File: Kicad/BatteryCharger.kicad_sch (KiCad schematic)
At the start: 25 parts, among them IC1 FS312F-G, Q30 FS8205

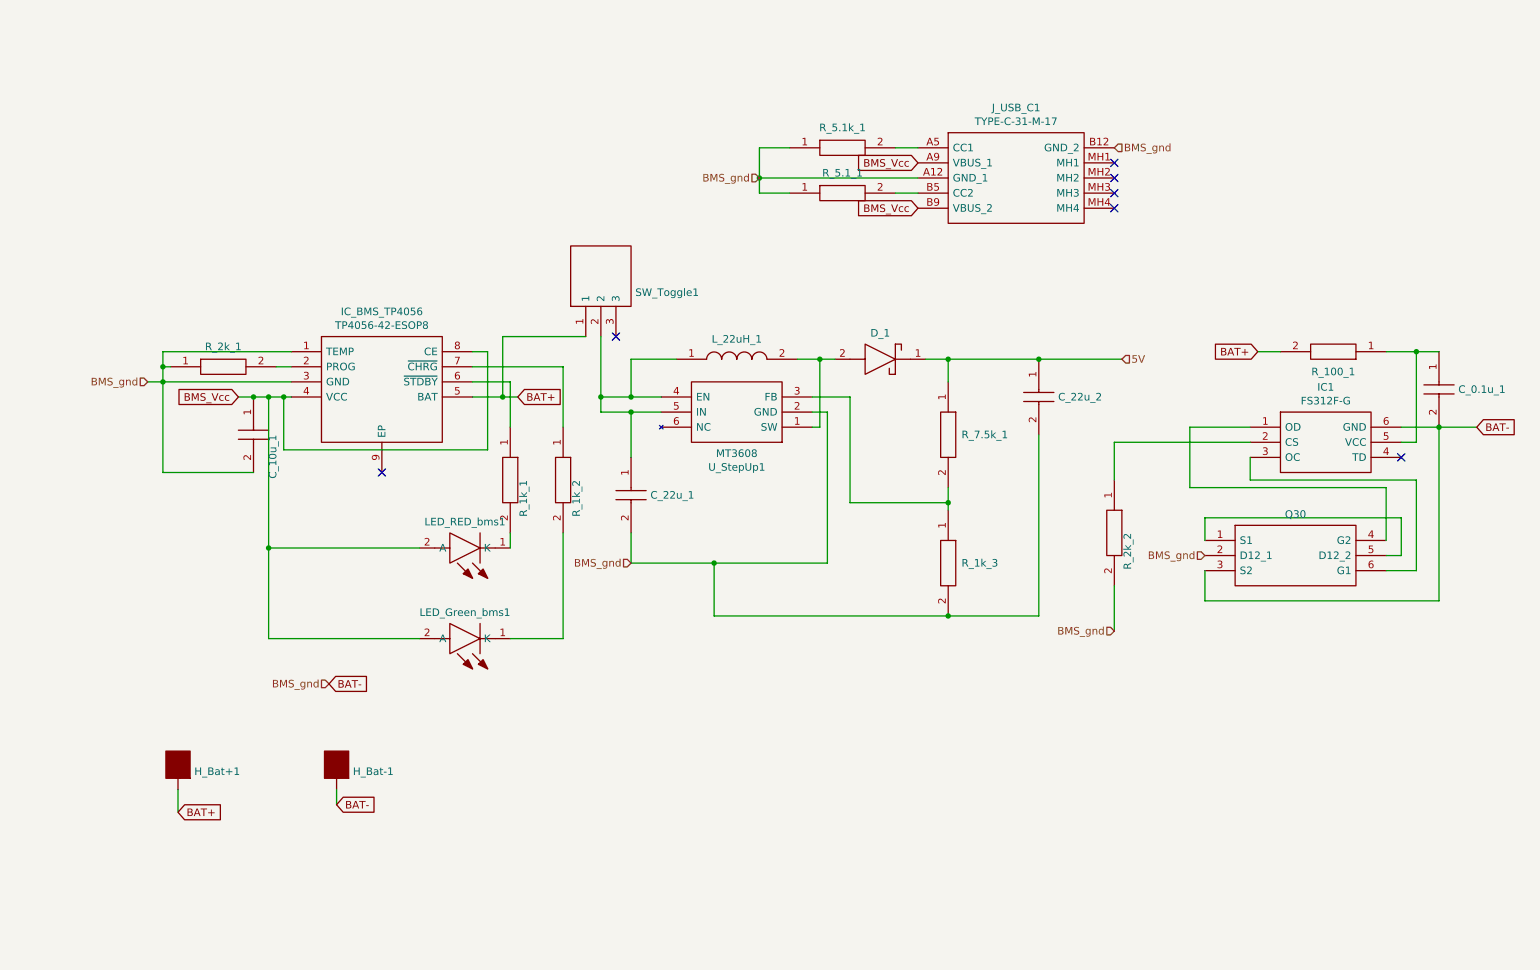
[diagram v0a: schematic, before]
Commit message: New V1.2 Hardware Release
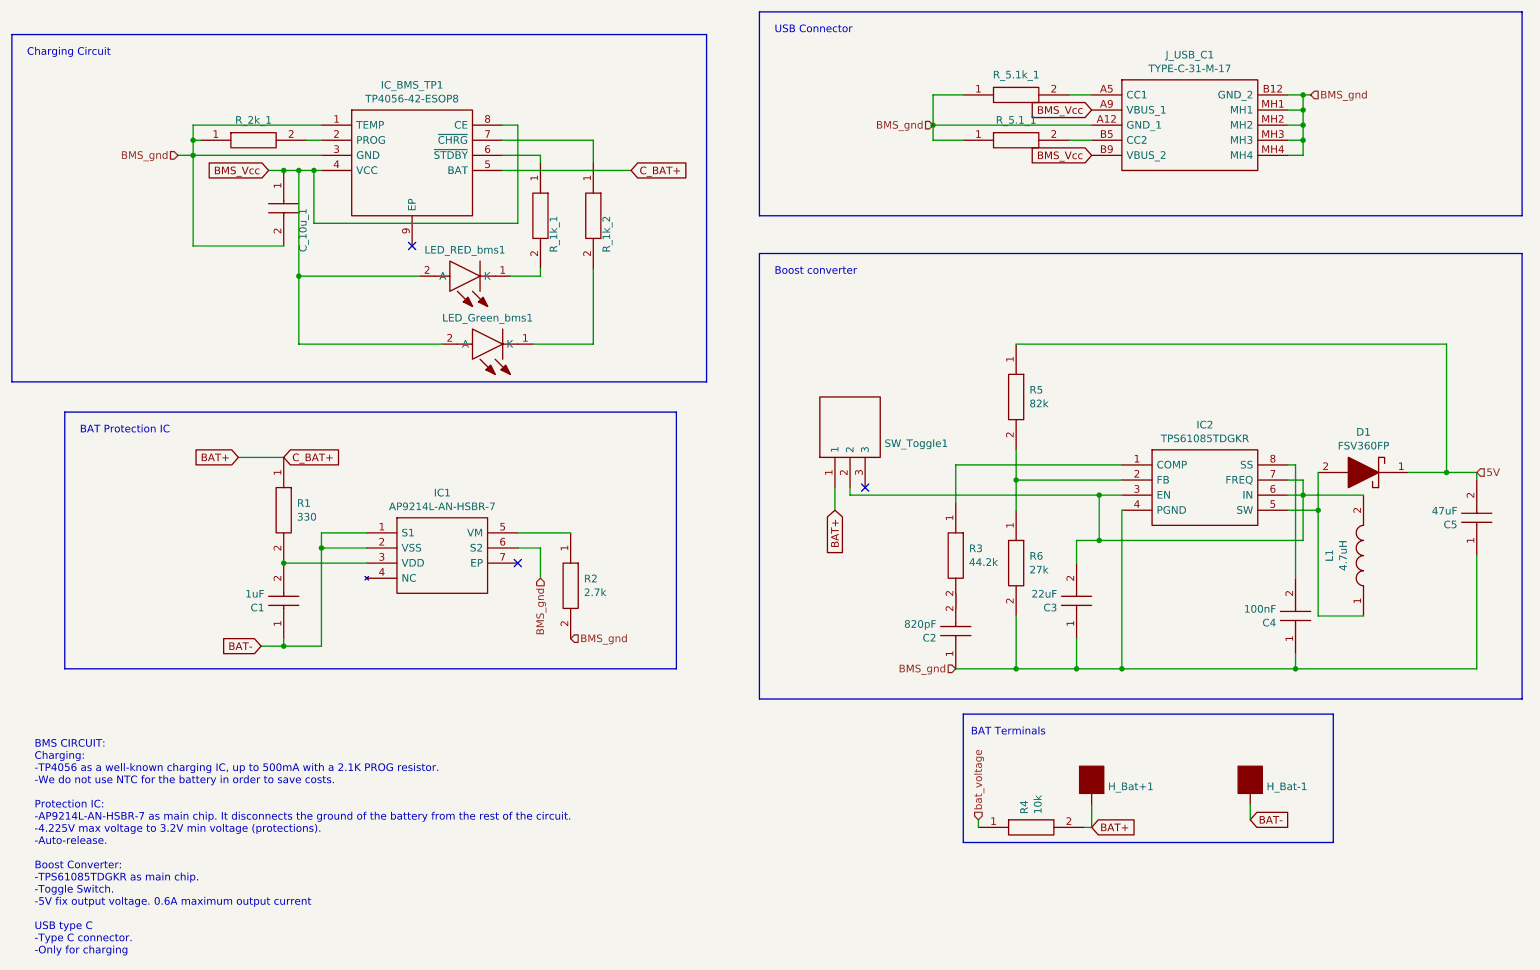
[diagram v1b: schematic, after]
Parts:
- removed C_0.1u_1, C_22u_1, C_22u_2: GCG21BR71H154KA01K, CAPC2012X145N, symbol PicBytesMicro-rescue:GCG21BR71H154KA01K-SamacSys_Parts
- removed D_1: SS34-E3_57T, DIOM7959X262N, symbol PicBytesMicro-rescue:SS34-E3_57T-SamacSys_Parts
- removed IC1: FS312F-G, SOT95P280X145-6N, symbol PicBytesMicro-rescue:FS312F-G-SamacSys_Parts
- removed L_22uH_1: SRR1260-220M, SRR1260-150M, symbol PicBytesMicro-rescue:SRR1260-220M-SamacSys_Parts
- removed Q30: FS8205, FS8205, symbol PicBytesMicro-rescue:FS8205-SamacSys_Parts
- removed R_100_1, R_1k_3, R_2k_2, R_7.5k_1: KTR10EZPF4220, RESC2012X65N, symbol PicBytesMicro-rescue:KTR10EZPF4220-SamacSys_Parts
- removed U_StepUp1: MT3608, SOT95P280X145-6N, symbol PicBytesMicro-rescue:MT3608-SamacSys_Parts
- added C1: 1uF, CAPC2012X140N, symbol Library_Loader:C0805C475M8RACTU
- added C2: 820pF, CAPC2012X140N, symbol Library_Loader:C0805C475M8RACTU
- added C3: 22uF, CAPC2012X140N, symbol Library_Loader:C0805C475M8RACTU
- added C4: 100nF, CAPC2012X140N, symbol Library_Loader:C0805C475M8RACTU
- added C5: 47uF, CAPC2012X140N, symbol Library_Loader:C0805C475M8RACTU
- added D1: FSV360FP, SS12FP, symbol Library_Loader:FSV360FP
- added IC1: AP9214L-AN-HSBR-7, AP9214LANHSBR7, symbol Library_Loader:AP9214L-AN-HSBR-7
- added IC2: TPS61085TDGKR, SOP65P490X110-8N, symbol Library_Loader:TPS61085TDGKR
- added L1: 4.7uH, SRN6045_1, symbol Library_Loader:SRN6045-4R7Y
- added R1: 330, RESC2012X75N, symbol Library_Loader:ERJP6WF1303V
- added R2: 2.7k, RESC2012X75N, symbol Library_Loader:ERJP6WF1303V
- added R3: 44.2k, RESC2012X75N, symbol Library_Loader:ERJP6WF1303V
- added R4: 10k, RESC2012X75N, symbol Library_Loader:ERJP6WF1303V
- added R5: 82k, RESC2012X75N, symbol Library_Loader:ERJP6WF1303V
- added R6: 27k, RESC2012X75N, symbol Library_Loader:ERJP6WF1303V
- renumbered IC_BMS_TP4056 to IC_BMS_TP1
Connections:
- net 5V: now also C5.2, D1.1, R5.1
- net BAT+: now also R1.1, R4.2
- net BAT-: now also C1.1, IC1.1 (S1), IC1.2 (VSS); no longer C_10u_1.2, IC_BMS_TP1.1 (TEMP), IC_BMS_TP1.3 (GND), J_USB_C1.A12 (GND_1), J_USB_C1.B12 (GND_2), R_2k_1.1, R_5.1_1.1, R_5.1k_1.1
- net BMS_gnd: now reaches J_USB_C1.MH1
- net BMS_gnd: now also C_10u_1.2, IC_BMS_TP1.1 (TEMP), IC_BMS_TP1.3 (GND), J_USB_C1.A12 (GND_1), J_USB_C1.B12 (GND_2), J_USB_C1.MH2, J_USB_C1.MH3, J_USB_C1.MH4, R_2k_1.1, R_5.1_1.1, R_5.1k_1.1, C2.1, C3.1, C4.1, C5.1, IC1.6 (S2), IC2.4 (PGND), R2.2, R6.2
- net at SW_Toggle1.2: now also C3.2, IC2.3 (EN), IC2.6 (IN), IC2.7 (FREQ), L1.2
- new net: IC1.5 (VM), R2.1
- new net: IC2.1 (COMP), R3.1
- new net: C2.2, R3.2
- new net: IC2.2 (FB), R5.2, R6.1
- new net: C4.2, IC2.8 (SS)
- new net: D1.2, IC2.5 (SW), L1.1
- new net: C1.2, IC1.3 (VDD), R1.2
- new net bat_voltage: R4.1
- no-connect marks 7 -> 3
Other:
- note added: "BAT Protection IC"
- note added: "BAT Terminals"
- note added: "BMS CIRCUIT: Charging: -TP4056 as a well-known charging IC, up to 500mA with a 2.1K PROG resistor. -We do not use NTC for the battery in order to save costs. Protection IC: -AP9214L-AN-HSBR-7 as main chip. It disconnects the ground of the battery from the rest of the circuit. -4.225V max voltage to 3.2V min voltage (protections). -Auto-release. Boost Converter: -TPS61085TDGKR as main chip. -Toggl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"
- note added: "Boost converter"
- note added: "Charging Circuit"
- note added: "USB Connector"
- company: (none) -> Making Devices
- title: (none) -> BMS
- moved on the sheet: C_10u_1, H_Bat+1, H_Bat-1, IC_BMS_TP1, J_USB_C1, LED_Green_bms1, LED_RED_bms1, R_1k_1, R_1k_2, R_2k_1, R_5.1_1, R_5.1k_1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
